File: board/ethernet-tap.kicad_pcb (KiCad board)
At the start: 4 copper layers, 139 x 92 mm, 409 parts, among them J1 BARREL_JACK, J10 XILINX_JTAG, J2 BEL_FUSE_0826-1G1T-23-F, J3 JUMPER_0402_SPDT, J4 JUMPER_0402_SPDT, J5 RJ45, J6 BEL_FUSE_0826-1G1T-23-F, J7 BEL_FUSE_0826-1G1T-23-F, J8 BEL_FUSE_0826-1G1T-23-F, J9 XILINX_JTAG, SW1 SWITCH, SW2 SWITCH, SW3 SWITCH, SW4 SWITCH, SW5 SWITCH, SW6 SWITCH, SW7 BUTTON, U1 LTC3374-QFN, U10 ECS-2016MVQ-250-CN-TR, U11 ECS-2016MVQ-250-CN-TR, U12 ECS-2016MVQ-250-CN-TR, U13 STM32H735-UFBGA176-25, U14 S25FLxxxS_BGA24_5x5_VIO, U2 KSZ9031RN, U3 MAX232, U4 XC7S15-1FTGB196C, U5 KSZ9031RN, U6 KSZ9031RN, U7 ECS-2016MVQ-250-CN-TR, U8 ECS-2016MVQ-250-CN-TR, U9 KSZ9031RN

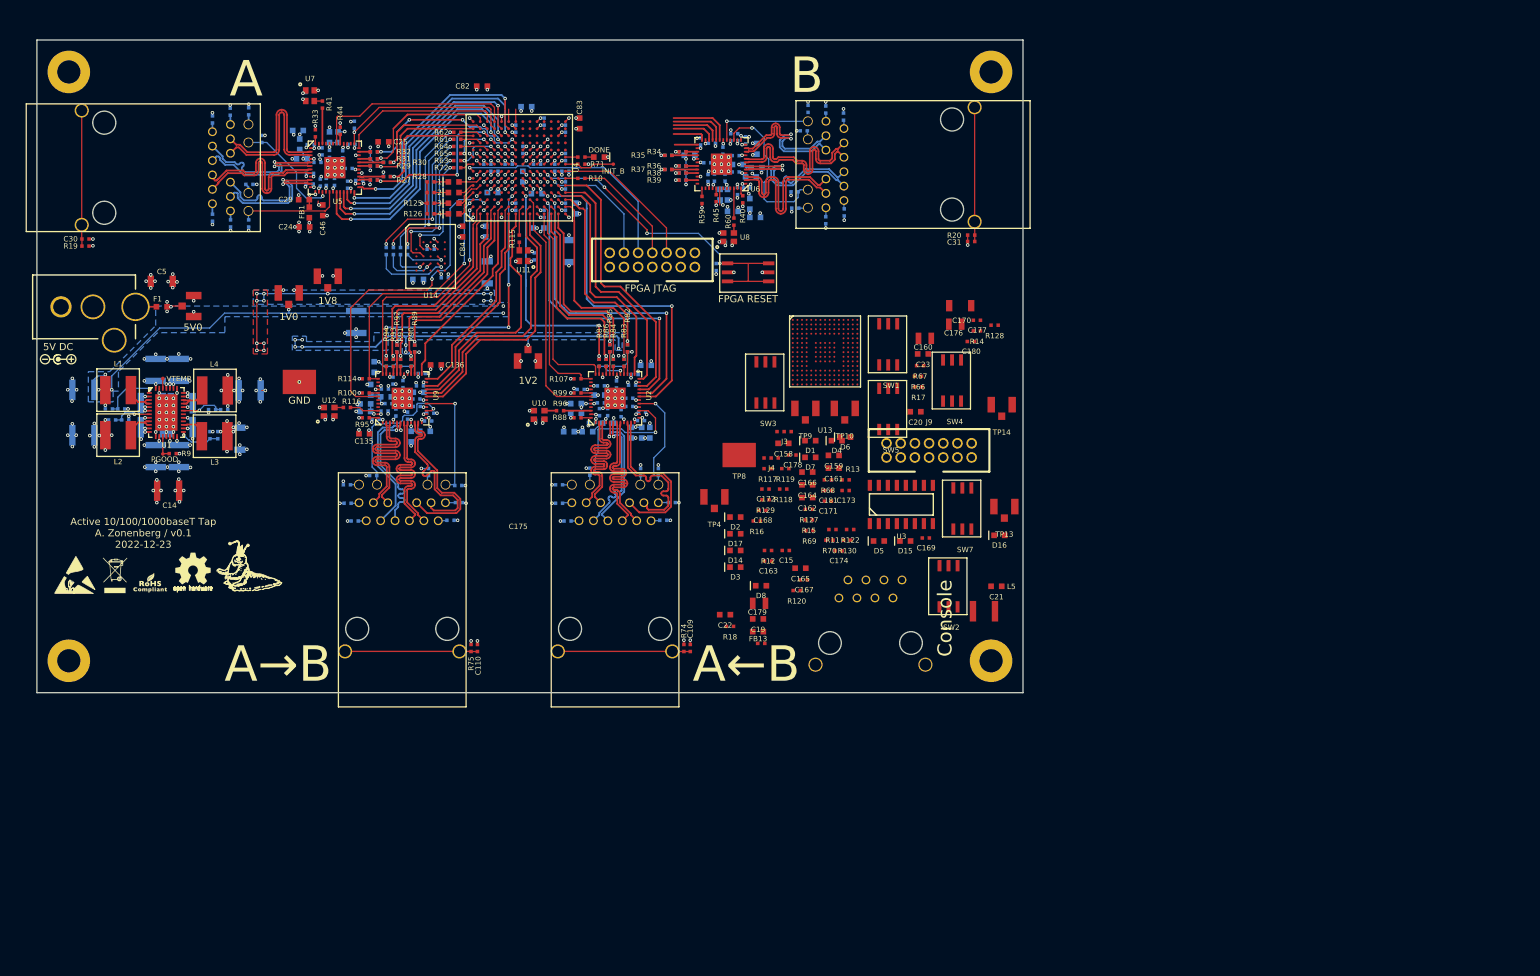
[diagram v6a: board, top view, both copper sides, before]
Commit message: Good progress on initial layout of MCU subsystem
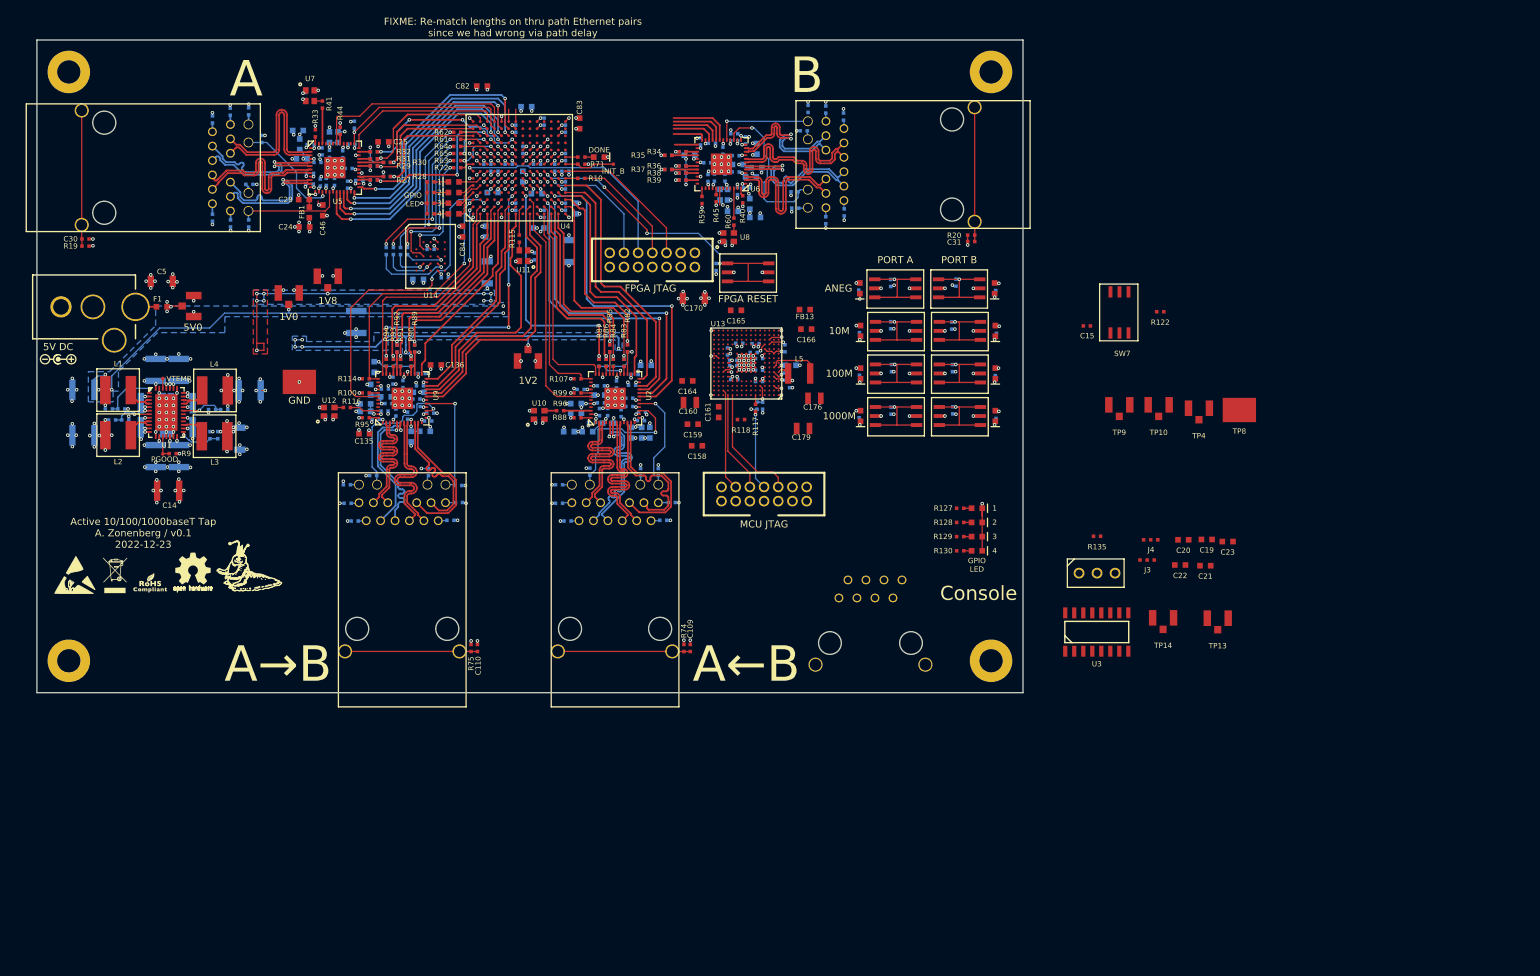
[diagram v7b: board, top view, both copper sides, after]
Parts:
- added J11: UART, azonenberg_pcb:CONN_HEADER_2.54MM_1x3, F.Cu at (170.4, 96.2)
- added R135: 0, azonenberg_pcb:EIA_0402_RES_NOSILK, F.Cu at (170.4, 91.0)
- added R136: 10K, azonenberg_pcb:EIA_0402_RES_NOSILK, B.Cu at (149.9, 61.2)
- added R137: 10K, azonenberg_pcb:EIA_0402_RES_NOSILK, B.Cu at (150.1, 67.2)
- added R138: 10K, azonenberg_pcb:EIA_0402_RES_NOSILK, B.Cu at (150.1, 73.2)
- added SW10: SWITCH, azonenberg_pcb:SWITCH_RAFI_MICON_5, F.Cu at (151.1, 74.0)
- added SW8: SWITCH, azonenberg_pcb:SWITCH_RAFI_MICON_5, F.Cu at (151.1, 62.0)
- added SW9: SWITCH, azonenberg_pcb:SWITCH_RAFI_MICON_5, F.Cu at (151.1, 68.0)
- C162, C163, C167, C168, C169, C171, C172, C173, C174, C175, C177, C178, C180, C181, R11, R119, R12, R120, R13, R14, R15, R16, R17, R18, R66, R67, R68, R69, R70: moved to B.Cu
- moved TP8 70.8 mm to (190.5, 73.2)
- moved TP4 69.4 mm to (184.8, 73.0)
- moved C22 64.5 mm to (182.2, 95.0)
- moved C19 64.2 mm to (185.9, 91.4)
- moved J4 54.7 mm to (178.0, 91.5)
- moved J3 54.3 mm to (177.5, 94.3)
- moved R122 53.4 mm to (179.3, 59.3)
- moved C15 52.9 mm to (169.0, 61.3)
- moved C23 50.4 mm to (188.8, 91.7)
- moved FB13 45.9 mm to (129.2, 59.0)
- moved TP10 44.3 mm to (179.1, 72.5)
- moved TP9 44.3 mm to (173.6, 72.5)
- moved L5 42.4 mm to (128.4, 68.0), turned to 180 degrees
- moved C20 41.8 mm to (182.6, 91.5)
- moved D8 40.8 mm to (156.1, 74.0), turned to 90 degrees
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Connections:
- net /Management Interface/1000M_SW renamed /Management Interface/LEFT_1000M_SW
- net /Management Interface/100M_SW renamed /Management Interface/LEFT_100M_SW
- net /Management Interface/10M_SW renamed /Management Interface/LEFT_10M_SW
- U13 pad M2: unconnected-(U13-PadM2) -> /Management Interface/RIGHT_10M_SW
- U13 pad N2: unconnected-(U13-PadN2) -> /Management Interface/RIGHT_100M_SW
- U13 pad R6: unconnected-(U13-PadR6) -> /Management Interface/RIGHT_1000M_SW
- U3 pad 12: /Management Interface/UART_RX -> Net-(U3-Pad12)
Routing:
- net /GND: track 1037.0 -> 1356.6 mm, vias 288 -> 343
- net /3V3: track 554.3 -> 723.2 mm, vias 85 -> 118
- net /Management Interface/MCU_JTAG_TDI: track 0.00 -> 16.9 mm
- net /Management Interface/LEFT_10M_SW: track 0.00 -> 14.7 mm, vias 0 -> 1
- net /Management Interface/LEFT_ANEG_SW: track 0.00 -> 14.7 mm, vias 0 -> 1
- net /Management Interface/RIGHT_ANEG_SW: track 0.00 -> 14.6 mm, vias 0 -> 1
- net /Management Interface/RIGHT_10M_SW: track 0.00 -> 14.6 mm, vias 0 -> 1
- net /Management Interface/LEFT_1000M_SW: track 0.00 -> 14.6 mm, vias 0 -> 1
- net /Management Interface/LEFT_100M_SW: track 0.00 -> 14.6 mm, vias 0 -> 1
- net /Management Interface/RIGHT_100M_SW: track 0.00 -> 14.6 mm, vias 0 -> 1
- net /Management Interface/RIGHT_1000M_SW: track 0.00 -> 14.6 mm, vias 0 -> 1
- net /Management Interface/MCU_JTAG_TMS: track 0.00 -> 14.3 mm
- net /Management Interface/MCU_JTAG_TCK: track 0.00 -> 14.2 mm
- net /Management Interface/MCU_JTAG_TDO: track 0.00 -> 11.1 mm, vias 0 -> 1
- net /Management Interface/VSMPS: track 0.00 -> 7.35 mm
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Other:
- board text added: "1000M"
- board text added: "100M"
- board text added: "10M"
- board text added: "ANEG"
- board text added: "FIXME: Re-match lengths on thru path Ethernet pairs since we had wrong via path delay"
- board text added: "GPIO LED"
- board text added: "MCU JTAG"
- board text added: "PORT A"
- board text added: "PORT B"

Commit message: Updating file: ethernet-tap.kicad_pcb with current fully routed design.
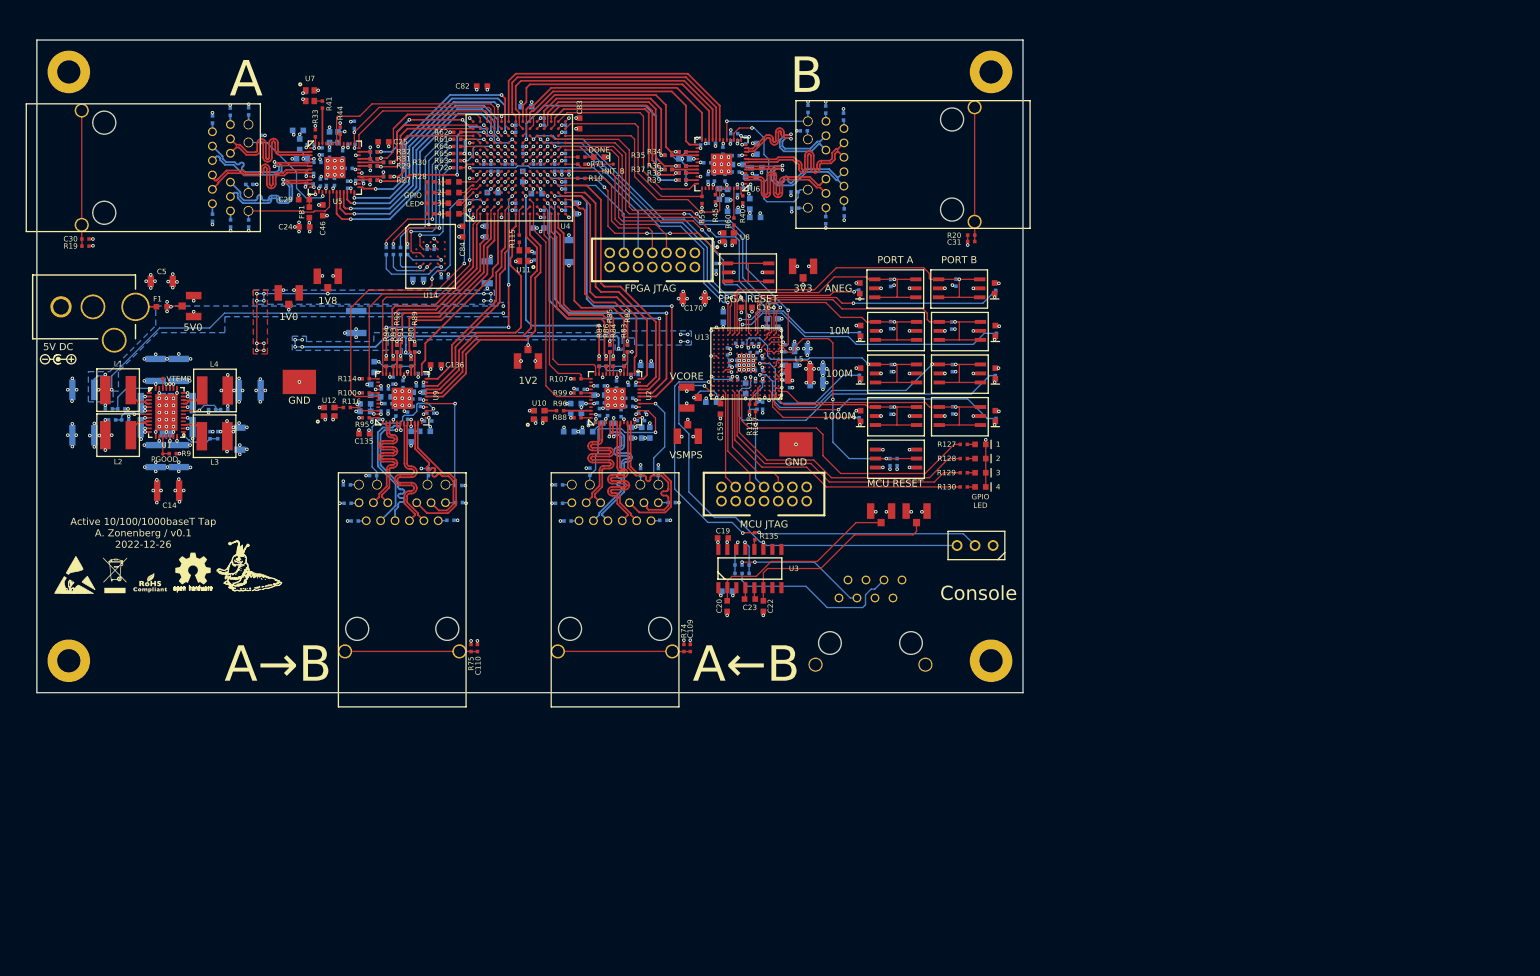
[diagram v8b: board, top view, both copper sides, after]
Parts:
- C15, C158, C160, C161, C165, C166, C176, C179, C21, FB13, J3, J4, R122: moved to B.Cu
- moved C19 68.2 mm to (117.7, 91.2)
- moved C23 67.8 mm to (121.5, 99.8)
- moved C21 67.5 mm to (118.3, 98.7)
- moved TP10 66.4 mm to (112.7, 71.4), turned to 90 degrees
- moved C20 65.0 mm to (118.3, 100.8), turned to -90 degrees
- moved TP8 62.7 mm to (128.0, 78.0)
- moved TP9 61.0 mm to (112.8, 76.8), turned to 180 degrees
- moved TP4 59.3 mm to (129.0, 53.0)
- moved C22 59.0 mm to (123.4, 100.8), turned to -90 degrees
- moved J4 57.8 mm to (120.4, 96.2), turned to 180 degrees
- moved J3 57.1 mm to (120.4, 95.0)
- moved U3 49.7 mm to (121.5, 95.5)
- moved R135 48.2 mm to (122.2, 91.0), turned to 90 degrees
- moved TP13 45.1 mm to (145.0, 87.5)
- moved R122 42.7 mm to (142.2, 80.5), turned to -90 degrees
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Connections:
- TP13 pad 1: /Management Interface/VCP_P -> /Management Interface/VCP_N
- TP14 pad 1: /Management Interface/VCP_N -> /Management Interface/VCP_P
- U13 pad A10: unconnected-(U13-PadA10) -> /Management Interface/MCU_LED2
- U13 pad A2: /Management Interface/LEFT_100M_EN -> /Management Interface/RIGHT_1000M_EN
- U13 pad A5: /Management Interface/RIGHT_10M_EN -> unconnected-(U13-PadA5)
- U13 pad A7: (no net) -> unconnected-(U13-PadA7)
- U13 pad A8: (no net) -> unconnected-(U13-PadA8)
- U13 pad A9: unconnected-(U13-PadA9) -> /Management Interface/MCU_LED0
- U13 pad B1: unconnected-(U13-PadB1) -> /Management Interface/RIGHT_1000M_SW
- U13 pad B10: unconnected-(U13-PadB10) -> /Management Interface/MCU_LED1
- U13 pad B11: unconnected-(U13-PadB11) -> /Management Interface/MCU_LED3
- U13 pad B12: (no net) -> unconnected-(U13-PadB12)
- U13 pad B2: unconnected-(U13-PadB2) -> /Management Interface/LEFT_1000M_SW
- U13 pad B5: /Management Interface/LEFT_10M_EN -> unconnected-(U13-PadB5)
- U13 pad B7: (no net) -> unconnected-(U13-PadB7)
- U13 pad C13: (no net) -> unconnected-(U13-PadC13)
- U13 pad C6: /Management Interface/RIGHT_ANEG_EN -> unconnected-(U13-PadC6)
- U13 pad C7: (no net) -> unconnected-(U13-PadC7)
- U13 pad C8: (no net) -> unconnected-(U13-PadC8)
- U13 pad D12: (no net) -> unconnected-(U13-PadD12)
- U13 pad D7: (no net) -> /Management Interface/RIGHT_100M_EN
- U13 pad D8: (no net) -> unconnected-(U13-PadD8)
- U13 pad F14: (no net) -> unconnected-(U13-PadF14)
- U13 pad F15: (no net) -> unconnected-(U13-PadF15)
- U13 pad F3: (no net) -> unconnected-(U13-PadF3)
- U13 pad F4: (no net) -> /Management Interface/RIGHT_100M_SW
- U13 pad G12: (no net) -> unconnected-(U13-PadG12)
- U13 pad G13: (no net) -> unconnected-(U13-PadG13)
- U13 pad G14: (no net) -> unconnected-(U13-PadG14)
- U13 pad G15: (no net) -> unconnected-(U13-PadG15)
- U13 pad G3: (no net) -> unconnected-(U13-PadG3)
- U13 pad H1: (no net) -> unconnected-(U13-PadH1)
- U13 pad H13: (no net) -> unconnected-(U13-PadH13)
- U13 pad H2: (no net) -> unconnected-(U13-PadH2)
- U13 pad H3: (no net) -> unconnected-(U13-PadH3)
- U13 pad H4: (no net) -> /Management Interface/LEFT_100M_EN
- U13 pad J1: (no net) -> unconnected-(U13-PadJ1)
- U13 pad J2: (no net) -> unconnected-(U13-PadJ2)
- U13 pad J3: (no net) -> unconnected-(U13-PadJ3)
- U13 pad J4: (no net) -> unconnected-(U13-PadJ4)
- U13 pad K1: (no net) -> unconnected-(U13-PadK1)
- U13 pad K14: /Management Interface/LEFT_100M_SW -> unconnected-(U13-PadK14)
- U13 pad K15: /Management Interface/LEFT_10M_SW -> unconnected-(U13-PadK15)
- U13 pad K3: (no net) -> unconnected-(U13-PadK3)
- U13 pad L15: /Management Interface/LEFT_ANEG_EN -> unconnected-(U13-PadL15)
- U13 pad L2: /Management Interface/LEFT_1000M_SW -> unconnected-(U13-PadL2)
- U13 pad M11: (no net) -> unconnected-(U13-PadM11)
- U13 pad M12: /Management Interface/MCU_LED2 -> unconnected-(U13-PadM12)
- U13 pad M13: (no net) -> unconnected-(U13-PadM13)
- U13 pad M14: (no net) -> unconnected-(U13-PadM14)
- U13 pad M15: /Management Interface/LEFT_ANEG_SW -> unconnected-(U13-PadM15)
- U13 pad M2: /Management Interface/RIGHT_10M_SW -> unconnected-(U13-PadM2)
- U13 pad M7: unconnected-(U13-PadM7) -> /Management Interface/LEFT_100M_SW
- U13 pad M8: /Management Interface/RIGHT_100M_EN -> unconnected-(U13-PadM8)
- U13 pad N10: (no net) -> unconnected-(U13-PadN10)
- U13 pad N11: (no net) -> unconnected-(U13-PadN11)
- U13 pad N12: /Management Interface/RIGHT_ANEG_SW -> unconnected-(U13-PadN12)
- U13 pad N13: (no net) -> unconnected-(U13-PadN13)
- U13 pad N14: (no net) -> unconnected-(U13-PadN14)
- U13 pad N15: (no net) -> unconnected-(U13-PadN15)
- U13 pad N2: /Management Interface/RIGHT_100M_SW -> unconnected-(U13-PadN2)
- U13 pad N4: (no net) -> /Management Interface/LEFT_10M_SW
- U13 pad N7: (no net) -> unconnected-(U13-PadN7)
- U13 pad N9: (no net) -> unconnected-(U13-PadN9)
- U13 pad P1: /Management Interface/FPGA_IRQ -> unconnected-(U13-PadP1)
- U13 pad P10: /Management Interface/RIGHT_1000M_EN -> /Management Interface/LEFT_10M_EN
- U13 pad P11: (no net) -> /Management Interface/RIGHT_ANEG_SW
- U13 pad P12: /Management Interface/MCU_LED0 -> /Management Interface/FPGA_IRQ
- U13 pad P13: /Management Interface/MCU_LED1 -> unconnected-(U13-PadP13)
- U13 pad P14: /Management Interface/MCU_LED3 -> unconnected-(U13-PadP14)
- U13 pad P15: (no net) -> unconnected-(U13-PadP15)
- U13 pad P4: (no net) -> unconnected-(U13-PadP4)
- U13 pad P6: unconnected-(U13-PadP6) -> /Management Interface/RIGHT_ANEG_EN
- U13 pad P8: (no net) -> unconnected-(U13-PadP8)
- U13 pad R10: (no net) -> /Management Interface/LEFT_ANEG_SW
- U13 pad R4: (no net) -> /Management Interface/RIGHT_10M_SW
- U13 pad R5: (no net) -> unconnected-(U13-PadR5)
- U13 pad R6: /Management Interface/RIGHT_1000M_SW -> /Management Interface/LEFT_ANEG_EN
- U13 pad R9: unconnected-(U13-PadR9) -> /Management Interface/RIGHT_10M_EN
- U4 pad F14: /Management Interface/FPGA_SPI_DQ3 -> /Thru Path/ETH1_RGMII_TXD0
- U4 pad G14: /Management Interface/FPGA_SPI_DQ2 -> /Thru Path/ETH1_RGMII_TXD1
- U4 pad H12: /Thru Path/ETH1_MDC -> /Thru Path/ETH1_RGMII_TX_CLK
- U4 pad H13: /Thru Path/ETH1_MDIO -> /Thru Path/ETH1_RGMII_TXD2
- U4 pad H14: /Thru Path/ETH1_RST_N -> /Thru Path/ETH1_RGMII_TXD3
- U4 pad J11: /Thru Path/ETH1_RGMII_TX_CLK -> unconnected-(U4-PadJ11)
- U4 pad J12: /Thru Path/ETH1_RGMII_TX_EN -> /Management Interface/FPGA_SPI_DQ1
- U4 pad J14: /Management Interface/FPGA_SPI_DQ0 -> /Thru Path/ETH1_RGMII_TX_EN
- U4 pad K12: /Management Interface/FPGA_SPI_SCK -> /Management Interface/FPGA_IRQ
- U4 pad L12: /Thru Path/ETH1_RGMII_TXD2 -> unconnected-(U4-PadL12)
- U4 pad L13: /Thru Path/ETH1_RGMII_TXD3 -> /Thru Path/ETH1_RGMII_RXD1
- U4 pad L14: /Thru Path/ETH1_RGMII_TXD1 -> /Thru Path/ETH1_RGMII_RXD2
- U4 pad M10: /Thru Path/ETH1_RGMII_RXD0 -> unconnected-(U4-PadM10)
- U4 pad M11: /Thru Path/ETH1_RGMII_RXD1 -> /Management Interface/FPGA_SPI_CS_N
- U4 pad M12: /Management Interface/FPGA_SPI_CS_N -> /Management Interface/FPGA_SPI_DQ2
- U4 pad M13: /Thru Path/ETH1_RGMII_TXD0 -> /Thru Path/ETH1_RGMII_RX_DV
- U4 pad M14: unconnected-(U4-PadM14) -> /Thru Path/ETH1_RGMII_RXD0
- U4 pad N10: unconnected-(U4-PadN10) -> /Management Interface/FPGA_SPI_DQ0
- U4 pad N14: /Thru Path/ETH1_RGMII_RXD2 -> /Thru Path/ETH1_MDC
- U4 pad P10: /Thru Path/ETH1_RGMII_RX_DV -> /Management Interface/FPGA_SPI_SCK
- U4 pad P11: /Management Interface/FPGA_SPI_DQ1 -> /Management Interface/FPGA_SPI_DQ3
- U4 pad P12: unconnected-(U4-PadP12) -> /Thru Path/ETH1_RST_N
- U4 pad P13: /Management Interface/FPGA_IRQ -> /Thru Path/ETH1_MDIO
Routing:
- net /GND: track 1356.6 -> 1487.1 mm, vias 343 -> 377
- net /3V3: track 723.2 -> 823.9 mm, vias 118 -> 127
- net /Management Interface/UART_RX: track 0.00 -> 66.2 mm, vias 0 -> 3
- net /Management Interface/UART_TX: track 0.00 -> 62.6 mm, vias 0 -> 2
- net /Management Interface/FPGA_SPI_DQ2: track 1.75 -> 57.2 mm, vias 0 -> 2
- net /Management Interface/FPGA_SPI_DQ0: track 0.00 -> 51.6 mm, vias 0 -> 2
- net /Management Interface/VSMPS: track 7.35 -> 58.7 mm, vias 0 -> 9
- net /Management Interface/FPGA_SPI_DQ3: track 1.75 -> 52.1 mm, vias 0 -> 2
- net /Management Interface/FPGA_SPI_SCK: track 0.00 -> 47.7 mm, vias 0 -> 2
- net /Management Interface/FPGA_SPI_DQ1: track 0.00 -> 47.5 mm, vias 0 -> 2
- net /Management Interface/RIGHT_100M_EN: track 0.00 -> 46.4 mm, vias 0 -> 1
- net /Management Interface/FPGA_IRQ: track 0.00 -> 45.1 mm, vias 0 -> 2
- net /Management Interface/MCU_LED3: track 0.00 -> 41.6 mm
- net /Management Interface/FPGA_SPI_CS_N: track 0.00 -> 41.0 mm, vias 0 -> 2
- net /Management Interface/MCU_LED1: track 0.00 -> 40.9 mm
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- added copper zone on In2.Cu, net /Monitor Path/ETH3_A1V2
- added copper zone on In2.Cu, net /Monitor Path/ETH3_A3V3
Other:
- board text added: "3V3"
- board text added: "Active 10/100/1000baseT Tap A. Zonenberg / v0.1 2022-12-26"
- board text added: "MCU RESET"
- board text added: "VCORE"
- board text added: "VSMPS"
- board text removed: "Active 10/100/1000baseT Tap A. Zonenberg / v0.1 2022-12-23"
- board text removed: "FIXME: Re-match lengths on thru path Ethernet pairs since we had wrong via path delay"
